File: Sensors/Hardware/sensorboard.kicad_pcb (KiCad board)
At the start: 4 copper layers, 120 x 50 mm, 301 parts, among them J1 RBUS, J10 1053131104, J11 1053131104, J12 1053131104, J13 1053131104, J14 1053131104, J15 USB_C_Receptacle_USB2.0, J16 Micro_SD_Card_Det, J3 1053131104, J4 1053131104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

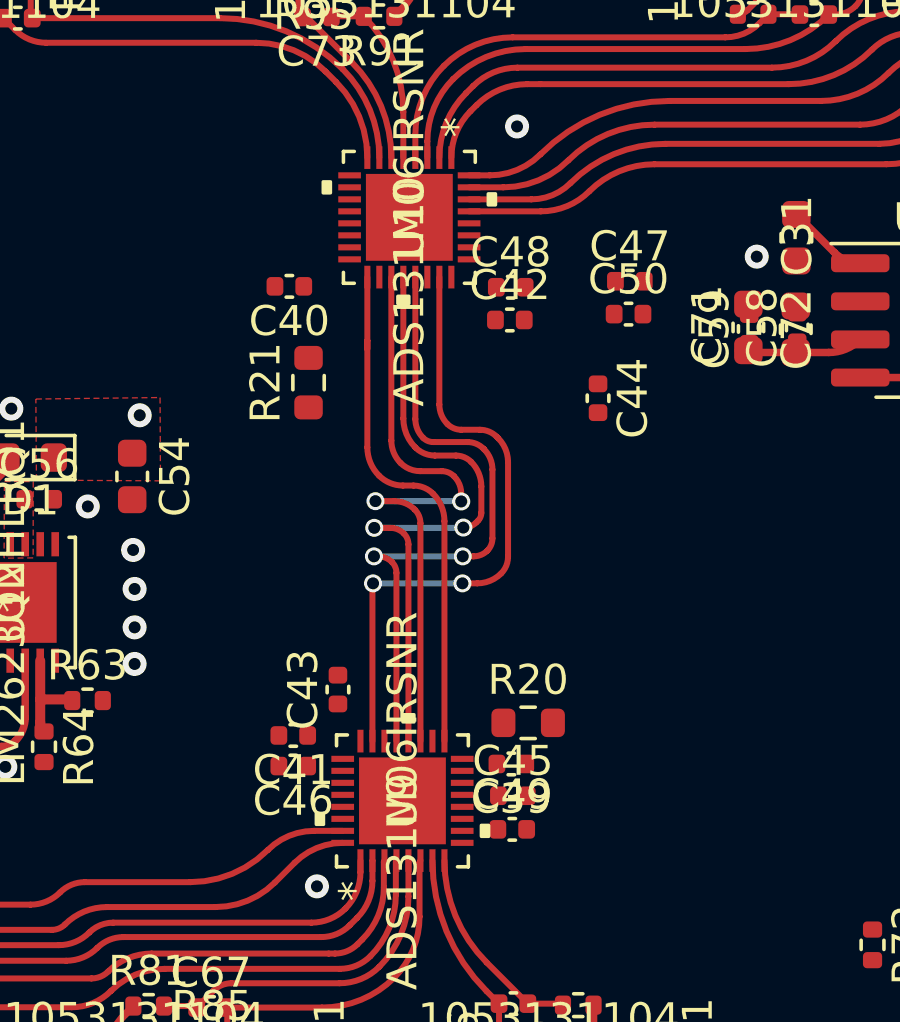
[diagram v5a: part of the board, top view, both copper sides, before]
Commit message: ADC connections and KiCAD version update
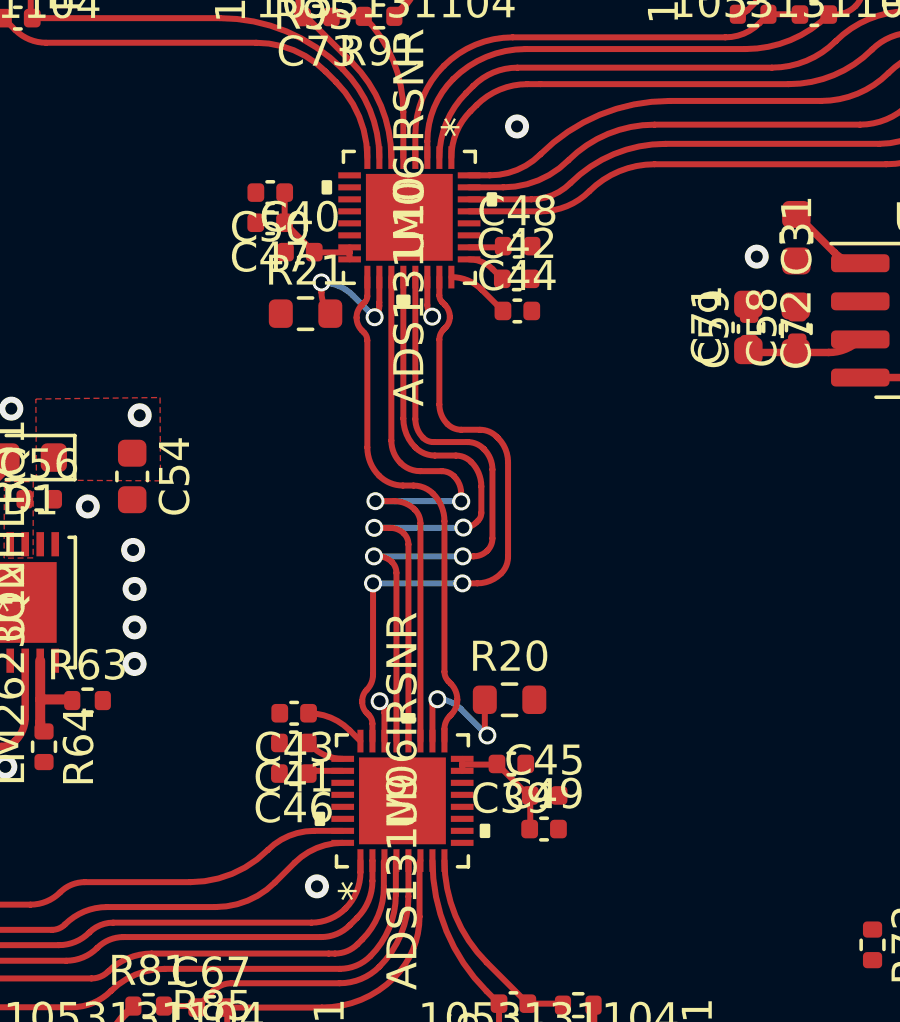
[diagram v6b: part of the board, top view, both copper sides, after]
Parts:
- moved C50 12.6 mm to (140.4, 44.5), turned to 180 degrees
- moved C47 12.1 mm to (140.4, 45.5), turned to 180 degrees
- moved C44 3.96 mm to (148.6, 48.4), turned to 0 degrees
- moved R21 2.30 mm to (141.6, 48.5), turned to 0 degrees
- moved C43 1.66 mm to (141.2, 61.8), turned to 180 degrees
- moved C48 1.39 mm to (148.6, 46.3)
- moved C42 1.39 mm to (148.6, 47.4)
- moved C40 1.19 mm to (141.4, 46.5), turned to 0 degrees
- moved C45 1.06 mm to (149.5, 64.6)
- moved C49 1.06 mm to (149.5, 65.7)
- moved R20 0.99 mm to (148.4, 61.4)
- moved C41 0.25 mm to (141.2, 62.8)
- moved C46 0.25 mm to (141.2, 63.8)
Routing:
- net +3V3: track 216.8 -> 227.3 mm
- net Net-(R20-Pad1): track 0.00 -> 4.79 mm, vias 0 -> 2
- net Net-(R21-Pad2): track 0.00 -> 4.70 mm, vias 0 -> 2
- net GND: track 11.4 -> 14.2 mm, vias 30 -> 32
- net Net-(C44-Pad1): track 0.00 -> 2.12 mm
- net Net-(C43-Pad1): track 0.00 -> 2.02 mm
- net Net-(C42-Pad1): track 0.00 -> 1.32 mm
- net Net-(C41-Pad1): track 0.00 -> 1.30 mm

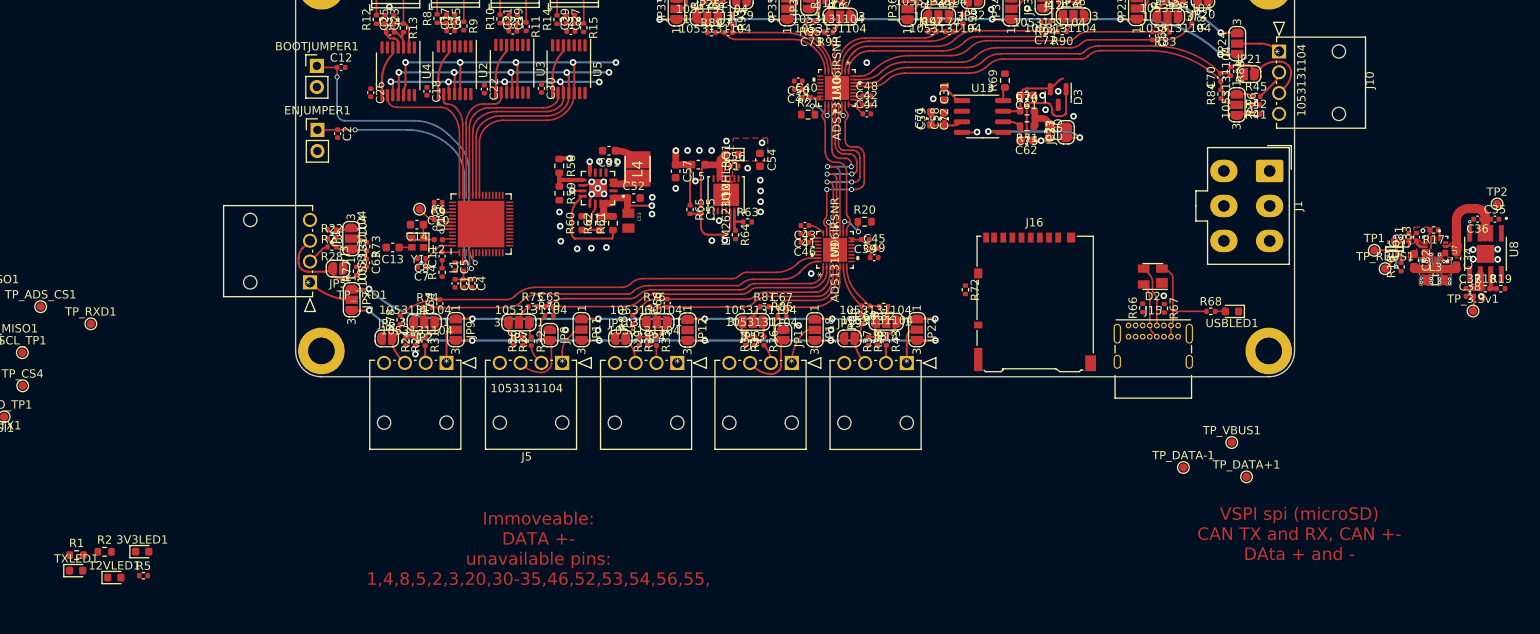
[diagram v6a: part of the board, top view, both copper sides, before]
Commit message: added LEDS and CAN connections
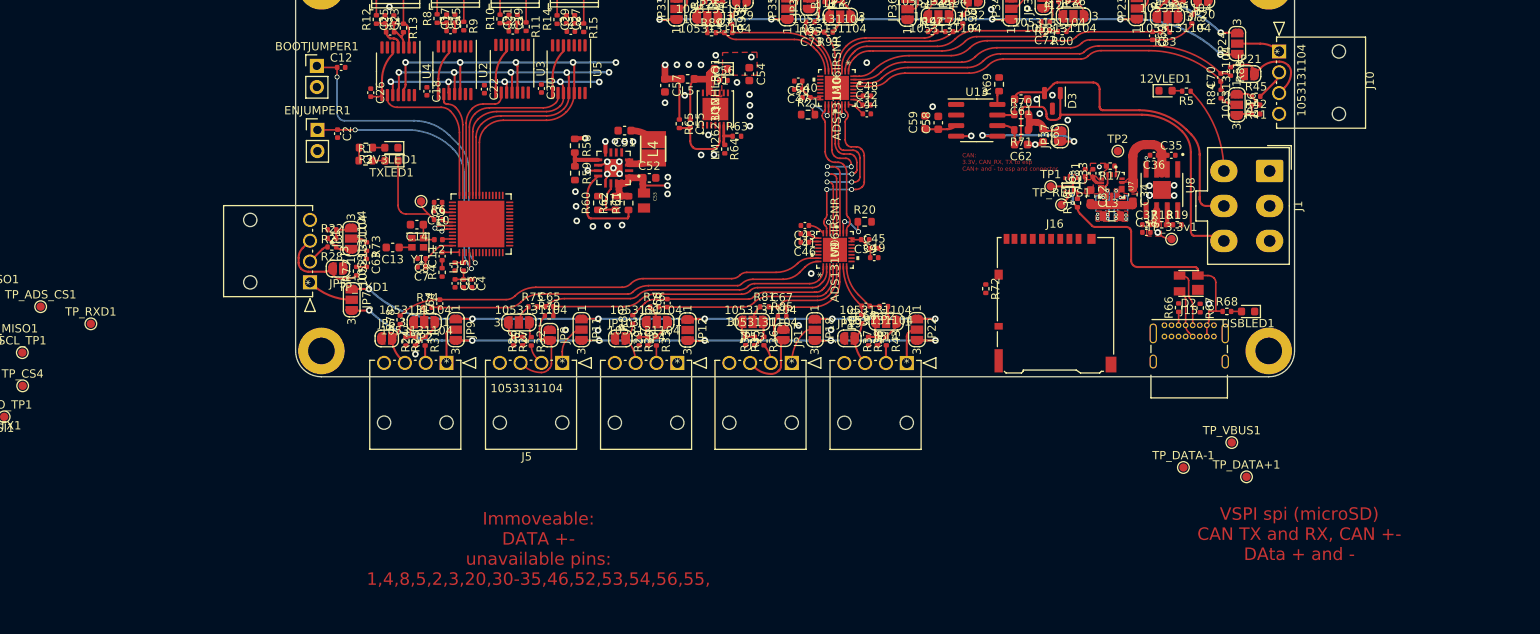
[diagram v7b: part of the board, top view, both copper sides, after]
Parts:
- removed the C31 at (157.9, 46.0)
- removed the C71 at (156.3, 49.0)
- removed the C72 at (157.9, 49.0)
- removed the C73 at (170.5, 50.5)
- removed the C74 at (167.8, 46.2)
- removed C75: 220 pF, Capacitor_SMD:C_0603_1608Metric
- C58, C59, C60, C61, C62: footprint Capacitor_SMD:C_0402_1005Metric -> Capacitor_SMD:C_0603_1608Metric
- moved 12VLED1 139.2 mm to (184.5, 45.6)
- moved R5 138.1 mm to (187.0, 45.7), turned to 180 degrees
- moved TXLED1 62.1 mm to (91.5, 54.0), turned to 180 degrees
- moved R1 58.7 mm to (88.4, 54.0)
- moved R2 57.8 mm to (88.4, 52.5), turned to 180 degrees
- moved 3V3LED1 57.0 mm to (91.5, 52.5), turned to 180 degrees
- moved TP2 46.0 mm to (178.8, 52.9)
- moved C33 39.6 mm to (175.8, 55.5)
- moved C34 39.6 mm to (180.6, 58.1)
- moved C37 39.6 mm to (182.2, 61.7)
- moved L3 39.6 mm to (178.0, 60.7)
- moved R16 39.6 mm to (173.9, 59.1)
- moved R18 39.6 mm to (184.0, 61.7)
- moved TP1 39.6 mm to (170.7, 57.1)
- moved U6 39.6 mm to (173.1, 57.0)
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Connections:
- R6 pad 1: Net-(R6-Pad1) -> /TXD
- TP_TXD1 pad 1: Net-(R6-Pad1) -> /TXD
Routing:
- net /CAN-: track 17.2 -> 49.1 mm
- net /CAN+: track 9.72 -> 41.3 mm
- net VBUS: track 18.3 -> 36.8 mm
- net /TXD: track 0.00 -> 12.4 mm
- net +12V: track 0.00 -> 10.6 mm
- net +3V3: track 227.3 -> 230.4 mm
- net /CAN_TX: track 2.74 -> 0.00 mm
- net Net-(R6-Pad1): track 2.20 -> 0.00 mm
- net Net-(J15-CC1): track 0.00 -> 1.61 mm
- net Net-(TXLED1-A): track 0.00 -> 1.51 mm
- net Net-(3V3LED1-A): track 0.00 -> 1.45 mm
- net Net-(12VLED1-A): track 0.00 -> 1.22 mm
- net /Data+: track 6.76 -> 6.00 mm
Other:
- board text added: "CAN: 3.3V, CAN_RX, TX to esp CAN+ and - to esp and connector"

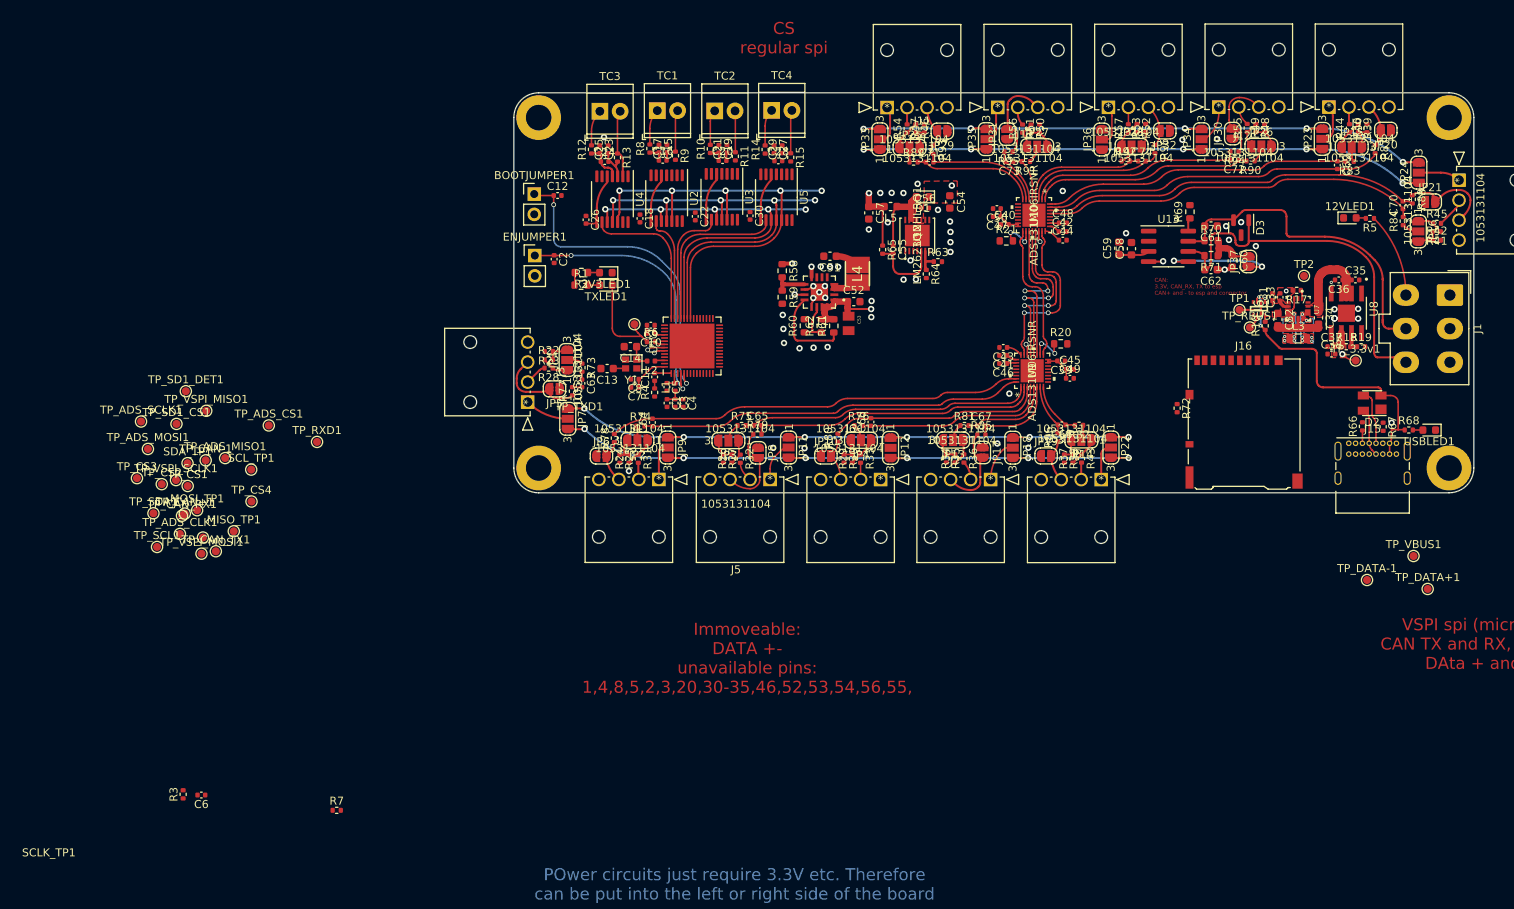
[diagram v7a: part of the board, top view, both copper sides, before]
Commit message: spacings and redo lines with tps
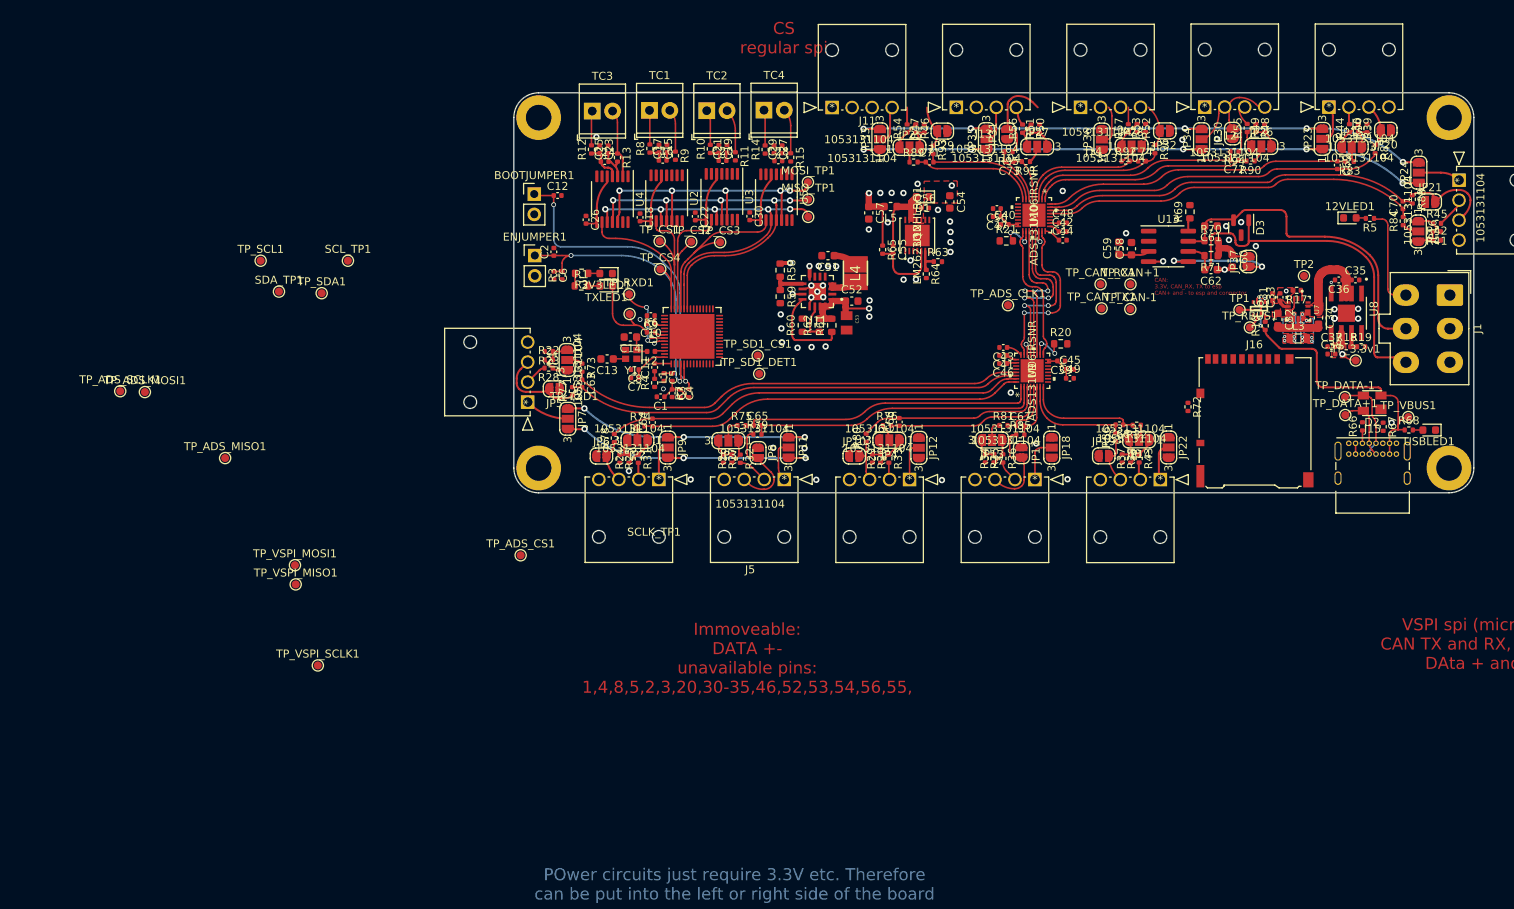
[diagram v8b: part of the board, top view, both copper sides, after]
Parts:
- moved TP_CAN+1 121.6 mm to (157.1, 53.9)
- moved TP_CAN_RX1 118.4 mm to (153.3, 53.9)
- moved TP_CAN-1 117.1 mm to (157.1, 57.0)
- moved TP_CAN_TX1 114.8 mm to (153.5, 57.0)
- moved TP_ADS_CLK1 107.4 mm to (141.8, 56.5)
- moved MOSI_TP1 86.7 mm to (116.8, 41.2)
- moved SCLK_TP1 85.6 mm to (116.8, 45.5)
- moved MISO_TP1 82.9 mm to (116.8, 43.3)
- moved R3 80.3 mm to (86.0, 52.8)
- moved TP_CS3 78.6 mm to (105.8, 48.7)
- moved C6 78.5 mm to (85.0, 52.8), turned to -90 degrees
- moved TP_SD1_CS1 73.2 mm to (110.5, 62.9)
- moved TP_CS2 72.8 mm to (102.2, 48.6)
- moved TP_SD1_DET1 71.7 mm to (110.7, 65.1)
- moved R7 68.3 mm to (101.9, 67.5), turned to 90 degrees
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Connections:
- TP_CS1 pad 1: /CS2 -> /CS0
- TP_CS2 pad 1: /CS3 -> /CS1
- TP_CS3 pad 1: /CS0 -> /CS2
- TP_CS4 pad 1: /CS1 -> /CS3
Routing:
- net /analogueSPI/AIN0N: track 1.19 -> 57.6 mm
- net /analogueSPI/AIN0P: track 0.97 -> 57.4 mm
- net +5V: track 171.8 -> 125.0 mm, vias 12 -> 9
- net +3V3: track 230.4 -> 189.4 mm, vias 16 -> 13
- net /MOSI: track 61.5 -> 39.4 mm
- net /analogueSPI/AIN5P: track 6.87 -> 14.7 mm
- net /analogueSPI/AIN5N: track 6.44 -> 14.0 mm
- net Net-(U1-U0RXD/PROG/GPIO44): track 2.19 -> 9.34 mm, vias 1 -> 2
- net Net-(JP12-C): track 0.00 -> 4.96 mm
- net /Data-: track 6.85 -> 10.8 mm
- net /analogueSPI/AIN4P: track 11.4 -> 7.41 mm
- net /analogueSPI/AIN4N: track 11.3 -> 7.32 mm
- net VBUS: track 36.8 -> 40.4 mm
- net /MISO: track 56.8 -> 53.4 mm
- net /CS0: track 13.4 -> 16.5 mm
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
